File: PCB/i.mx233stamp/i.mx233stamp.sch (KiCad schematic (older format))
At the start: 0 parts

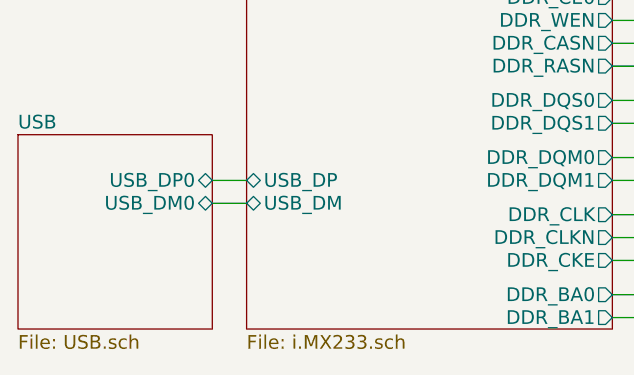
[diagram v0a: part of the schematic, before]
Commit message: Ruteo de la mayoría de los componentes, sin la alimentación
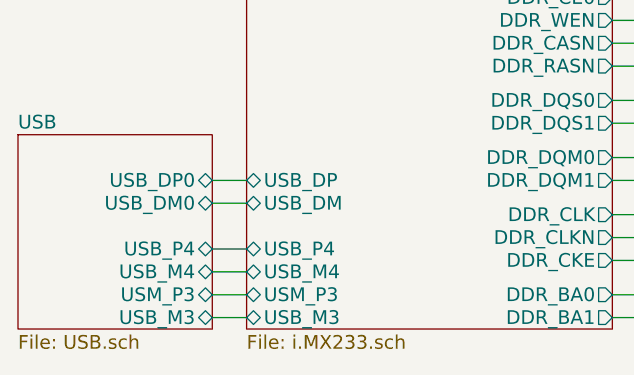
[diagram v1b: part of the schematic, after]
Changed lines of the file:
@@
-EESchema Schematic File Version 2  date Thu 11 Aug 2011 02:37:53 PM COT
+EESchema Schematic File Version 2  date Fri 12 Aug 2011 11:16:45 AM COT
 LIBS:con-jack
 LIBS:adm3101e
@@
 LIBS:mcp130
 LIBS:ABM8G
+LIBS:usb_a
 LIBS:i.mx233stamp-cache
 EELAYER 25  0
@@
 Sheet 1 4
 Title ""
-Date "11 aug 2011"
+Date "12 aug 2011"
 Rev ""
 Comp ""
@@
 $EndDescr
 Wire Wire Line
+	3000 4050 3150 4050
+Wire Wire Line
+	3000 3850 3150 3850
+Wire Wire Line
 	3000 3550 3150 3550
 Wire Wire Line
@@
 Wire Wire Line
 	3150 3450 3000 3450
+Wire Wire Line
+	3000 3750 3150 3750
+Wire Wire Line
+	3000 3950 3150 3950
 $Sheet
 S 2150 3250 850  850
@@
 F2 "USB_DM0" T R 3000 3550 60
 F3 "USB_DP0" T R 3000 3450 60
+F4 "USB_P4" B R 3000 3750 60
+F5 "USB_M4" B R 3000 3850 60
+F6 "USM_P3" B R 3000 3950 60
+F7 "USB_M3" B R 3000 4050 60
 $EndSheet
 $Sheet
@@
 F24 "USB_DM" B L 3150 3550 60
 F25 "USB_DP" B L 3150 3450 60
+F26 "USB_M3" B L 3150 4050 60
+F27 "USM_P3" B L 3150 3950 60
+F28 "USB_M4" B L 3150 3850 60
+F29 "USB_P4" B L 3150 3750 60
 $EndSheet
 $EndSCHEMATC
